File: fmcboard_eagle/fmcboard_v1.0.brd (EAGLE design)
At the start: 98 x 74 mm, 64 parts, among them IC1 OPA699ID, IC2 OPA699ID, IC3 ICL7660CPA, IC4 ICL7660CPA, IC5 LM358, J1 8pin, J12 4p-2.54, J2 ASP-134604-01, J3 4p-2.54, J4 4p-2.54, J5 8pin, J6 4p-2.54, J7 8pin, Q1 BSS138, Q2 BSS138, Q3 BSS138, Q4 BSS138

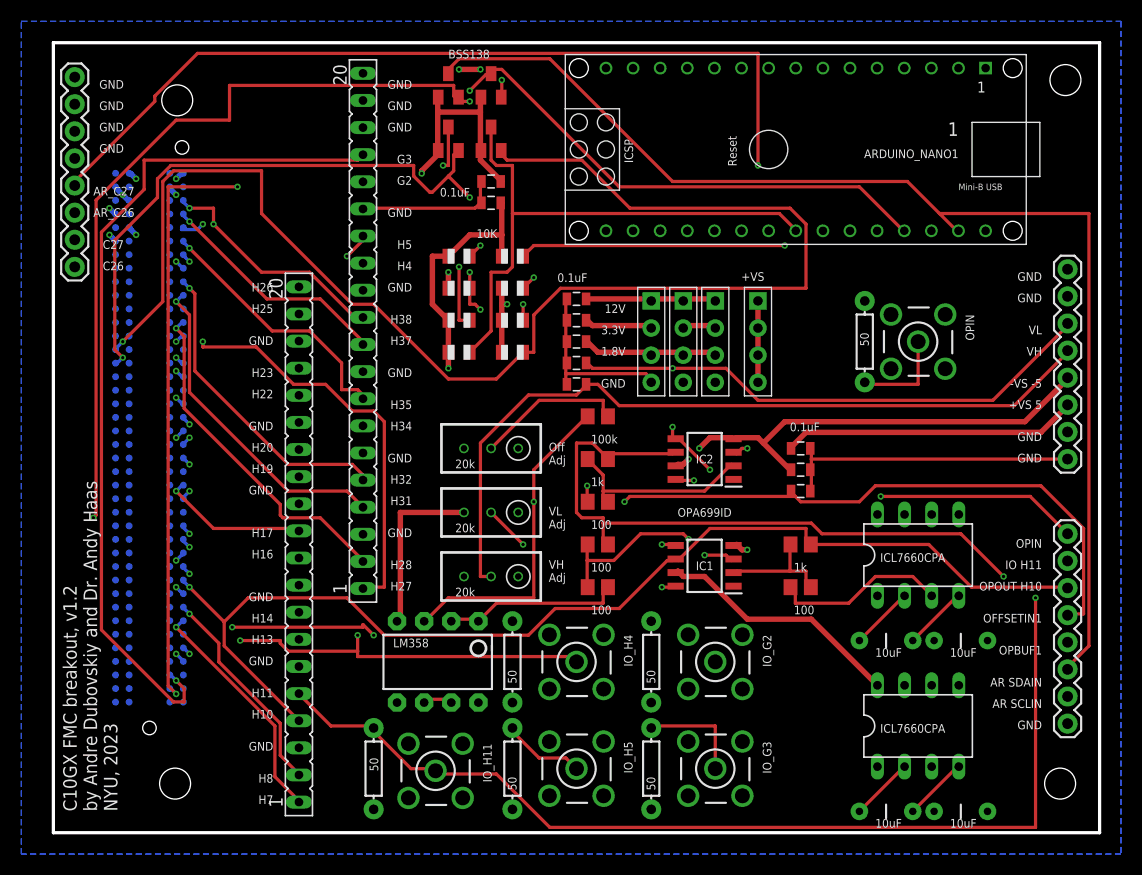
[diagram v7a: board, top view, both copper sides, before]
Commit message: Revert "switch to C26 and C27"
This reverts commit 01cab55b1ab11df4a8fa88617da78cc3c47528a8.
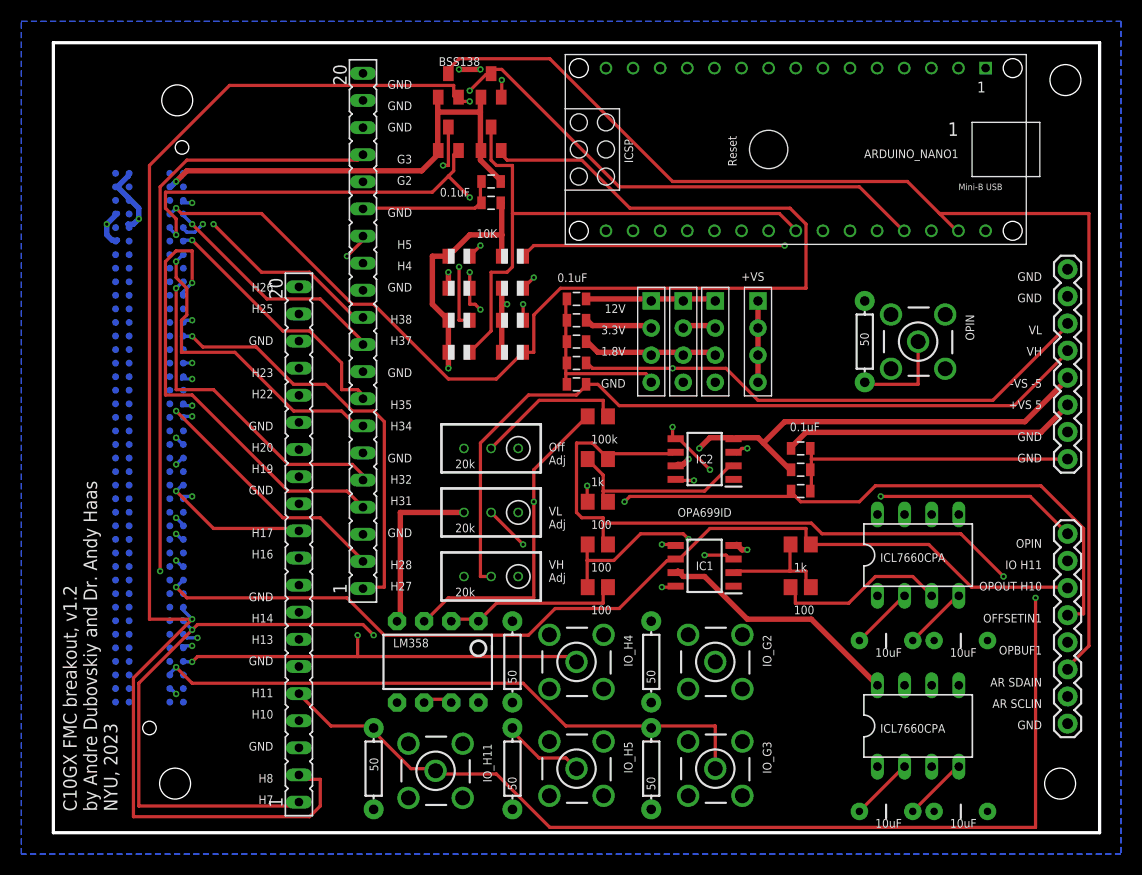
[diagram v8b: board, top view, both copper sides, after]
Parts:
- removed J7: 8pin, SparkFun-Connectors:1X08
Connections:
- removed net AR_C26: ARDUINO_NANO1.24, J7.3, Q3.3, R21.2
- removed net AR_C27: ARDUINO_NANO1.23, J7.4, Q4.3, R23.2
- removed net C26: J2.C26, J7.1, Q3.2, R22.2
- removed net C27: J2.C27, J7.2, Q4.2, R24.2
- new net AR_G36: ARDUINO_NANO1.24, Q3.3, R21.2
- new net AR_G37: ARDUINO_NANO1.23, Q4.3, R23.2
- new net G36: J2.G36, Q3.2, R22.2
- new net G37: J2.G37, Q4.2, R24.2
- net GND: no longer J7.5, J7.6, J7.7, J7.8
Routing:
- net C27: track 143.2 -> 0.00 mm, vias 1 -> 0
- net AR_C27: track 140.3 -> 0.00 mm, vias 1 -> 0
- net AR_C26: track 119.2 -> 0.00 mm, vias 2 -> 0
- net G37: track 0.00 -> 109.6 mm, vias 0 -> 1
- net C26: track 79.2 -> 0.00 mm, vias 3 -> 0
- net AR_G36: track 0.00 -> 73.2 mm, vias 0 -> 2
- net AR_G37: track 0.00 -> 52.6 mm
- net G36: track 0.00 -> 51.7 mm, vias 0 -> 3
- net G3: track 147.2 -> 123.8 mm, vias 1 -> 2
- net SDAIN: track 125.9 -> 146.6 mm, vias 4 -> 3
- net 1V8: track 101.1 -> 118.3 mm, vias 5 -> 3
- net H31: track 30.6 -> 42.9 mm
- net SCLIN: track 103.9 -> 115.9 mm, vias 6 -> 5
- net OPOUT1_H10: track 106.5 -> 114.3 mm
- net H34: track 35.1 -> 30.1 mm
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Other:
- board text removed: "AR_C26"
- board text removed: "AR_C27"
- board text removed: "C26"
- board text removed: "C27"
